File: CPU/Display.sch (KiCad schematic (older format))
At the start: 29 parts, among them IC5 MAX803, U1 CAT24C32, U2 STMPE811, U3 FAN5333BSX, X1 DISP_LCD_3.5IN_320X480_50PIN

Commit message: Replacing the TFT. Before removing EEPROM and voltage monitor.
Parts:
- removed C16: 10uF, Capacitor_SMD:C_0805_2012Metric_Pad1.15x1.40mm_HandSolder, symbol PiTFT-eagle-import:CAP_CERAMIC0805-NOOUTLINE
- removed C18: 0.1uF, Capacitor_SMD:C_0805_2012Metric_Pad1.15x1.40mm_HandSolder, symbol PiTFT-eagle-import:CAP_CERAMIC0805-NOOUTLINE
- removed C20: 1uF, Capacitor_SMD:C_0805_2012Metric_Pad1.15x1.40mm_HandSolder, symbol PiTFT-eagle-import:CAP_CERAMIC_0805MP
- removed D1: MM3Z24VT1G, PiTFT:SMADIODE, symbol PiTFT-eagle-import:DIODESMA
- removed D2: MBR0540, PiTFT:SOD-123, symbol PiTFT-eagle-import:DIODESOD-123
- removed L1: 10uH 1007, PiTFT:INDUCTOR_1007, symbol PiTFT-eagle-import:INDUCTOR
- removed R1: 12Ω, Resistor_SMD:R_0805_2012Metric_Pad1.15x1.40mm_HandSolder, symbol CPU-eagle-import:R-US_R1206
- removed R10, R9: 1K, Resistor_SMD:R_0805_2012Metric_Pad1.15x1.40mm_HandSolder, symbol CPU-eagle-import:R-US_R1206
- removed R11, R2, R7: 10K, Resistor_SMD:R_0805_2012Metric_Pad1.15x1.40mm_HandSolder, symbol CPU-eagle-import:R-US_R1206
- removed R8: DNP, Resistor_SMD:R_0805_2012Metric_Pad1.15x1.40mm_HandSolder, symbol PiTFT-eagle-import:RESISTOR0805_NOOUTLINE
- removed SJ2: SOLDERJUMPERCLOSED, PiTFT:SOLDERJUMPER_CLOSEDWIRE, symbol PiTFT-eagle-import:SOLDERJUMPERCLOSED
- removed U2: STMPE811, PiTFT:QFN16_3MM, symbol PiTFT-eagle-import:STMPE610
- removed U3: FAN5333BSX, PiTFT:SOT23-5@1, symbol PiTFT-eagle-import:FAN5331
- added Q401: IRLML0040TR, CPU:SOT23, symbol CPU-eagle-import:IRLML0040TR
- X1: footprint PiTFT:TFT_3.5IN_320X480_50PIN -> CPU:TFT_3.5IN_320X480_50PIN_BUY_DISPLAY_ER-TFT035-6; symbol PiTFT-eagle-import:DISP_LCD_3.5IN_320X480_50PIN -> MarcoK:DISP_LCD_3.5IN_320X480_50PIN_BUY_DISPLAY_ER-TFT035-6
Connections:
- net labels added: LCD_BACKLIGHT
- net labels removed: +24V, GPIO23, LCD_LITE, LEDK, Pi5V
- wire segments 129 -> 77
- no-connect marks 9 -> 7
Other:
- note removed: "7 x 3.2V LED boost"
- moved on the sheet: IC5, R12, R13, R14, R6, SJ1, U1

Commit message: BuyDisplay LCD.
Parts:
- removed IC5: MAX803, PiTFT:SOT23, symbol PiTFT-eagle-import:AXP083-SAG
- removed R12, R13, R14: 3.9K, Resistor_SMD:R_0805_2012Metric_Pad1.15x1.40mm_HandSolder, symbol CPU-eagle-import:R-US_R1206
- removed R6: 10K, Resistor_SMD:R_0805_2012Metric_Pad1.15x1.40mm_HandSolder, symbol CPU-eagle-import:R-US_R1206
- removed SJ1: SOLDERJUMPERCLOSED, PiTFT:SOLDERJUMPER_CLOSEDWIRE, symbol PiTFT-eagle-import:SOLDERJUMPER_CLOSED
- removed U1: CAT24C32, PiTFT:SOIC8_150MIL, symbol PiTFT-eagle-import:EEPROM_I2C_SOIC8_GENERIC
- added R401: 10, Resistor_SMD:R_0805_2012Metric_Pad1.15x1.40mm_HandSolder, symbol CPU-eagle-import:R-US_R1206
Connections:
- net +3V3: now also R401.2; no longer X1.1 (LEDA)
- new net: R401.1, X1.1 (LEDA)
- no-connect marks 7 -> 11

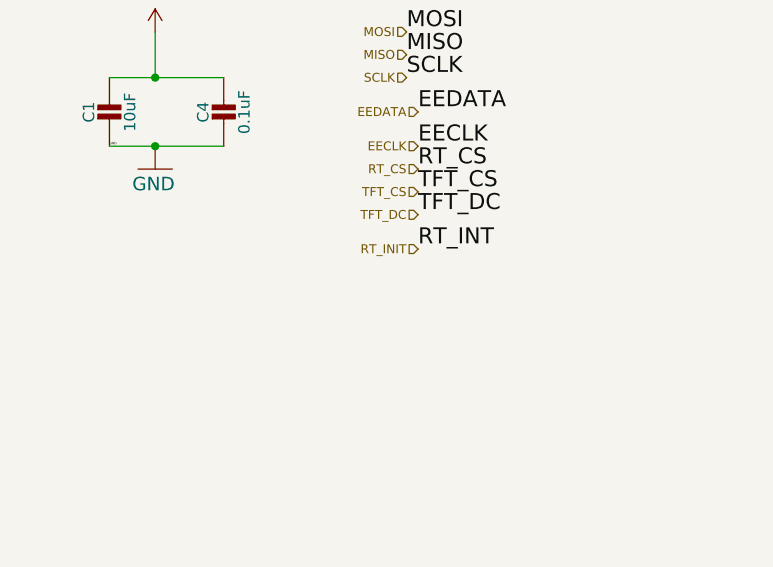
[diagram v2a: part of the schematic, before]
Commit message: Version 4 of the CPU board ordered with this commit.
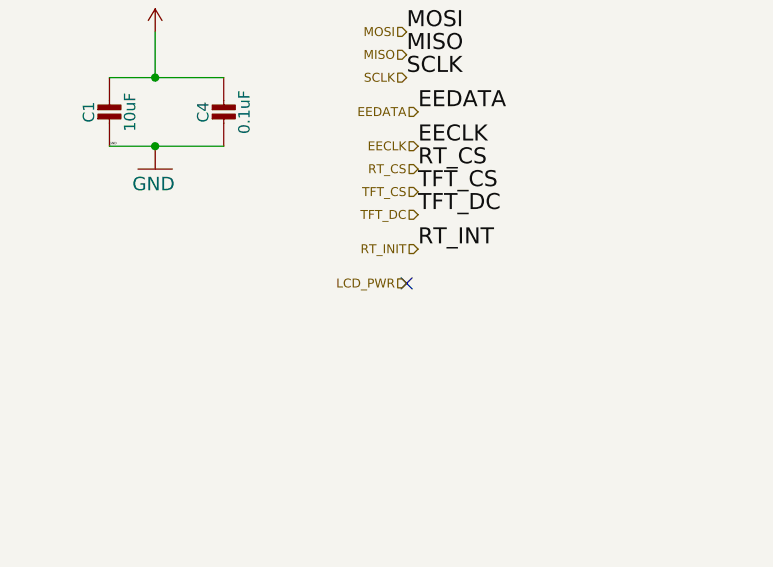
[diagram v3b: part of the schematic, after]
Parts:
- R3, R4, R401: LCSC Part Number C17414 -> C17415
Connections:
- no-connect marks 11 -> 12
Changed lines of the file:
@@
 F 2 "Resistor_SMD:R_0805_2012Metric_Pad1.15x1.40mm_HandSolder" H 10200 6000 50  0001 C CNN
 F 3 "" H 10200 6000 50  0001 C CNN
-F 4 " C17414" H 10200 6000 50  0001 C CNN "LCSC Part Number"
+F 4 "C17415" H 10200 6000 50  0001 C CNN "LCSC Part Number"
 F 5 "311-12.0CRCT-ND" H 10200 6000 50  0001 C CNN "DigiKey"
 F 6 "CR101-V3" H 10200 6000 50  0001 C CNN "Customer Reference"
@@
 F 2 "Resistor_SMD:R_0805_2012Metric_Pad1.15x1.40mm_HandSolder" H 10200 6200 50  0001 C CNN
 F 3 "" H 10200 6200 50  0001 C CNN
-F 4 " C17414" H 10200 6200 50  0001 C CNN "LCSC Part Number"
+F 4 "C17415" H 10200 6200 50  0001 C CNN "LCSC Part Number"
 F 5 "311-12.0CRCT-ND" H 10200 6200 50  0001 C CNN "DigiKey"
 F 6 "CR101-V3" H 10200 6200 50  0001 C CNN "Customer Reference"
@@
 F 2 "Resistor_SMD:R_0805_2012Metric_Pad1.15x1.40mm_HandSolder" H 6800 4700 50  0001 C CNN
 F 3 "" H 6800 4700 50  0001 C CNN
-F 4 " C17414" H 6800 4700 50  0001 C CNN "LCSC Part Number"
+F 4 "C17415" H 6800 4700 50  0001 C CNN "LCSC Part Number"
 F 5 "RC0805FR-0710KL" H 6800 4700 50  0001 C CNN "DigiKey"
 F 6 "CR101-V3" H 6800 4700 50  0001 C CNN "Customer Reference"
@@
 NoConn ~ 7700 4200
 NoConn ~ 7700 4300
+Text HLabel 2200 2000 0    39   Input ~ 0
+LCD_PWR
+NoConn ~ 2200 2000
 $EndSCHEMATC
